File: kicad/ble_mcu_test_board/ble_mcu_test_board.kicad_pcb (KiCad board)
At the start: 2 copper layers, 28 parts, among them J1 I2C_MUX_OUT, J2 SWD, SW1 SW_SPDT, SW2 SW_Push, U1 STM32WB10CCUx, U2 DLF162500LT-5028A1, U3 AMS1117-3.3, U4 TCA9548APWR

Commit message: prototype schematic + pcb finalized and ordered
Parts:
- added AE1: Antenna, pcb_antenna:meander_antenna_stm32wb10cc, F.Cu at (163.0, 85.8)
- added J3: USB_C_Receptacle_PowerOnly_6P, Connector_USB:USB_C_Receptacle_HRO_TYPE-C-31-M-17, F.Cu at (116.5, 85.5)
- added L1: 2.7n, Inductor_SMD:L_0402_1005Metric, F.Cu at (158.5, 85.7)
- added R1: 4k7, Resistor_SMD:R_0603_1608Metric, F.Cu at (128.9, 93.0)
- added R2: 4k7, Resistor_SMD:R_0603_1608Metric, F.Cu at (121.2, 93.0)
- added R3: 4k7, Resistor_SMD:R_0402_1005Metric, F.Cu at (122.5, 104.2)
- added R5: 5k1, Resistor_SMD:R_0603_1608Metric, F.Cu at (123.0, 85.0)
- added R6: 5k1, Resistor_SMD:R_0603_1608Metric, F.Cu at (123.0, 86.8)
- added Y1: 32MHz, Crystal:Crystal_SMD_2016-4Pin_2.0x1.6mm, F.Cu at (154.8, 81.4)
- R4: footprint Resistor_SMD:R_0402_1005Metric_Pad0.72x0.64mm_HandSolder -> Resistor_SMD:R_0402_1005Metric
- SW1: footprint Button_Switch_SMD:SW_SPDT_PCM12 -> external_footprints:SW_SSSS811101
- moved C11 29.8 mm to (155.6, 87.6), turned to -90 degrees
- moved U3 24.7 mm to (128.8, 85.5), turned to -90 degrees
- moved C2 21.3 mm to (156.9, 81.8), turned to 90 degrees
- moved J2 21.2 mm to (142.3, 89.9), turned to -90 degrees
- moved SW2 20.3 mm to (159.6, 92.9)
- moved U1 18.5 mm to (150.5, 87.0)
- moved C1 17.9 mm to (152.4, 81.5), turned to -90 degrees
- moved C4 17.7 mm to (146.8, 81.7)
- moved C7 17.5 mm to (151.2, 81.7)
- moved C5 17.4 mm to (145.8, 89.2)
- moved C3 17.1 mm to (150.9, 92.4), turned to -90 degrees
- moved C19 16.0 mm to (124.0, 82.0), turned to 90 degrees
- moved C8 14.8 mm to (147.9, 81.7)
- moved C18 14.4 mm to (124.0, 89.9), turned to -90 degrees
- moved C9 13.9 mm to (149.0, 81.7)
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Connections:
- U1 pad 39: Net-(J2-Pin_2) -> Net-(J2-Pin_3)
- U1 pad 41: Net-(J2-Pin_3) -> Net-(J2-Pin_2)
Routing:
- net +3.3V: track 2.54 -> 222.8 mm, vias 0 -> 7
- net GND: track 3.07 -> 76.0 mm, vias 2 -> 38
- net Net-(U1-PB9): track 9.02 -> 44.1 mm, vias 0 -> 2
- net BOOT0: track 0.00 -> 33.2 mm
- net Net-(U1-PB8): track 8.51 -> 41.3 mm
- net VBUS: track 0.00 -> 20.2 mm
- net Net-(J2-Pin_3): track 0.00 -> 12.7 mm
- net Net-(J2-Pin_2): track 0.00 -> 9.64 mm
- net Net-(U1-PA6): track 0.00 -> 9.60 mm
- net Net-(U4-*RESET): track 0.00 -> 9.58 mm
- net Net-(U1-OSC_IN): track 0.00 -> 5.11 mm
- net Net-(U1-OSC_OUT): track 0.00 -> 4.51 mm
- net RF_OUT: track 0.00 -> 4.09 mm
- net +3.3VA: track 0.00 -> 3.21 mm
- net Net-(J3-CC2): track 0.00 -> 2.81 mm
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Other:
- board outline added: 61.8 x 32.9 mm
- board text added: "C4,8,9,10,7,1"
- board text added: "I2C/VDCG"
- board text added: "POSTURE BEST C6_FL24_PB_v1.0"
- board text added: "SWD/GCDV"

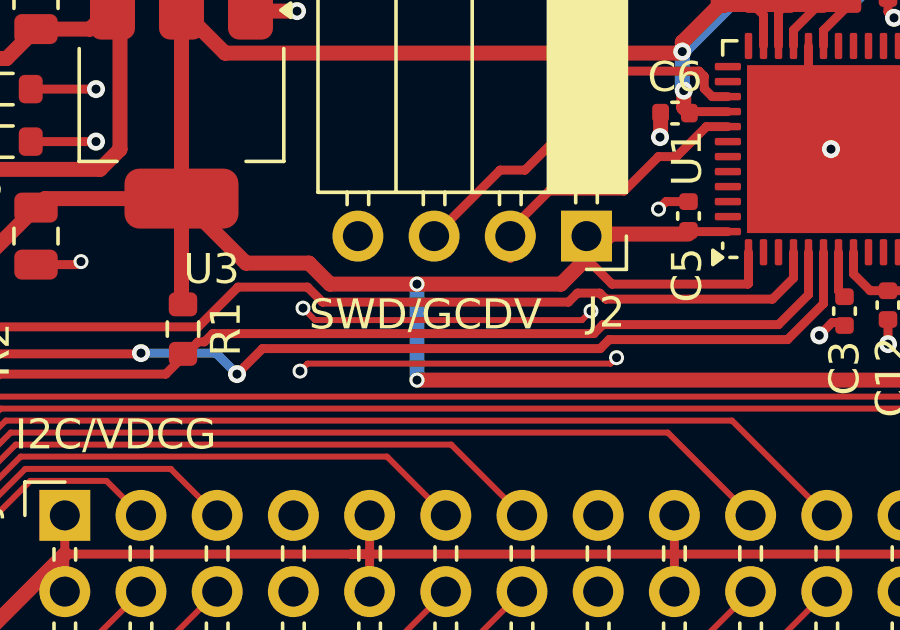
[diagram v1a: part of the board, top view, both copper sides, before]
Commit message: ble and i2c mux example code in stm32cubeide/ble_testing
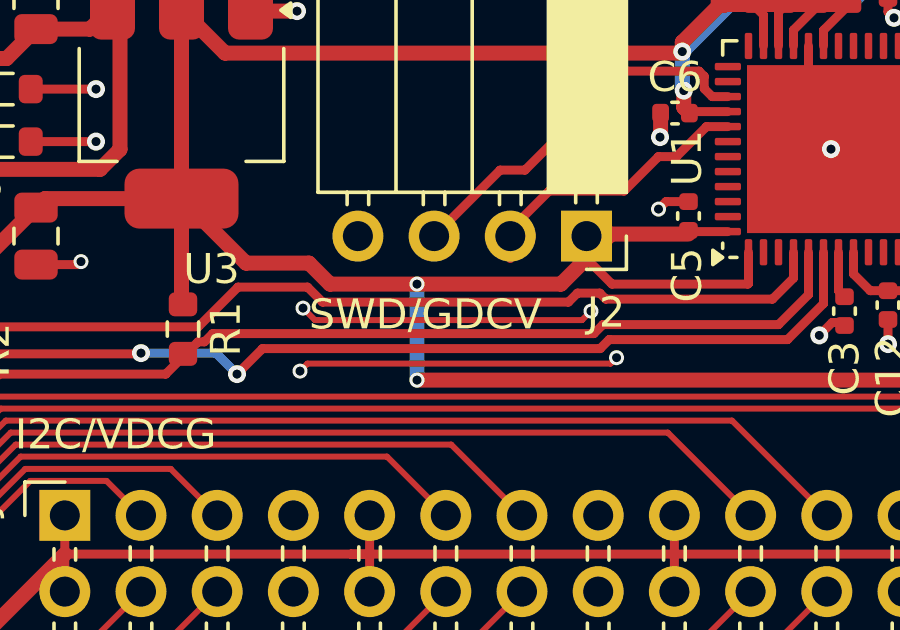
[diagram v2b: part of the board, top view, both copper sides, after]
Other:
- board text added: "SWD/GDCV"
- board text removed: "SWD/GCDV"
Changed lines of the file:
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@@
 		)
 	)
-	(gr_text "SWD/GCDV"
+	(gr_text "SWD/GDCV"
 		(at 133.1 93.1 0)
 		(layer "F.SilkS")

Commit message: Revert "ble and i2c mux example code in stm32cubeide/ble_testing"
This reverts commit 00b30e45b3f9405408dd6880b6cf67d626e086a2.
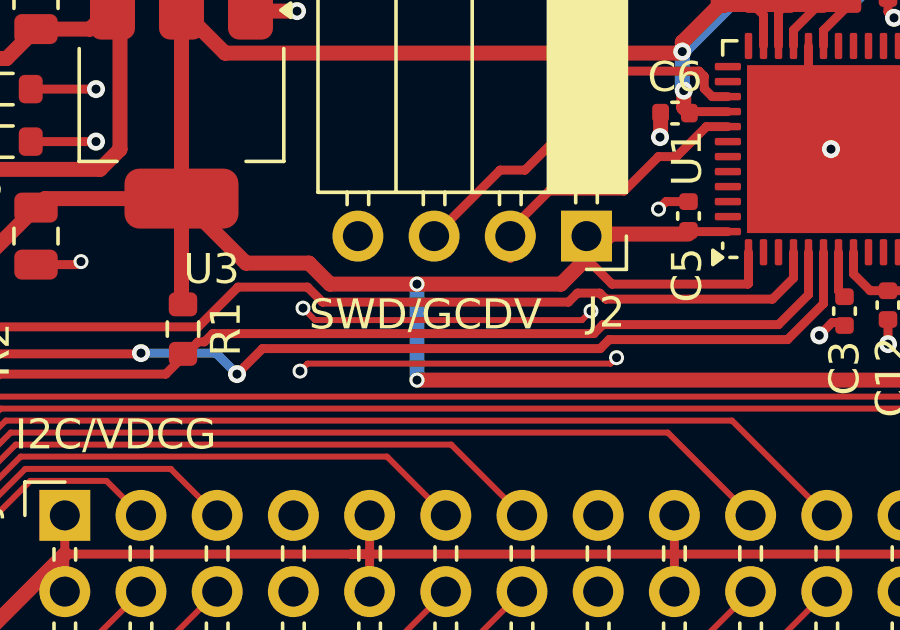
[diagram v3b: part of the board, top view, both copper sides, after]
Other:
- board text added: "SWD/GCDV"
- board text removed: "SWD/GDCV"
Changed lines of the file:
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@@
 		)
 	)
-	(gr_text "SWD/GDCV"
+	(gr_text "SWD/GCDV"
 		(at 133.1 93.1 0)
 		(layer "F.SilkS")
